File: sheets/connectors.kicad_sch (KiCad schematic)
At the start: 9 parts

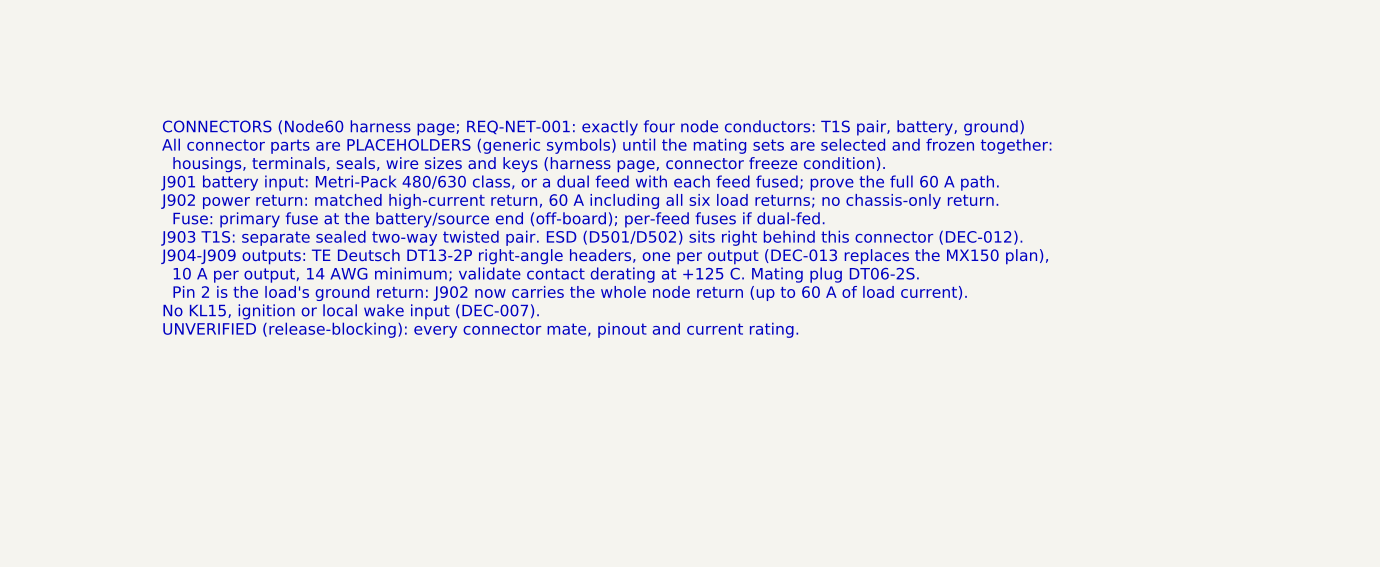
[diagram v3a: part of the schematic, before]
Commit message: Schematic: LHI to the MCU, current notes, net-name map
- LHI on all three TPS2HCS08 is now SW_LHI from S32K344 PTE4 (the
  architecture's GPIO list), still held low by the 10k pull-downs
  through reset.
- Page 4 cites NXP HDG Rev E2 Table 33 for unused GPIO, EXTAL/XTAL and
  the RESET_B pull-up instead of an open 'confirm' note.
- Copper notes for the 10 A output paths (p6) and the 60 A path (p2,
  p9), as IPC-2221 starting estimates to confirm with IPC-2152.
- interfaces.mdx maps the architecture's signal names to the schematic
  nets (RESET_L, T1S_IRQ_L, *_FLT_L, SPI4/SPI2/I2C0 buses).

Co-Authored-By: Claude Opus 5.5 <noreply@anthropic.com>
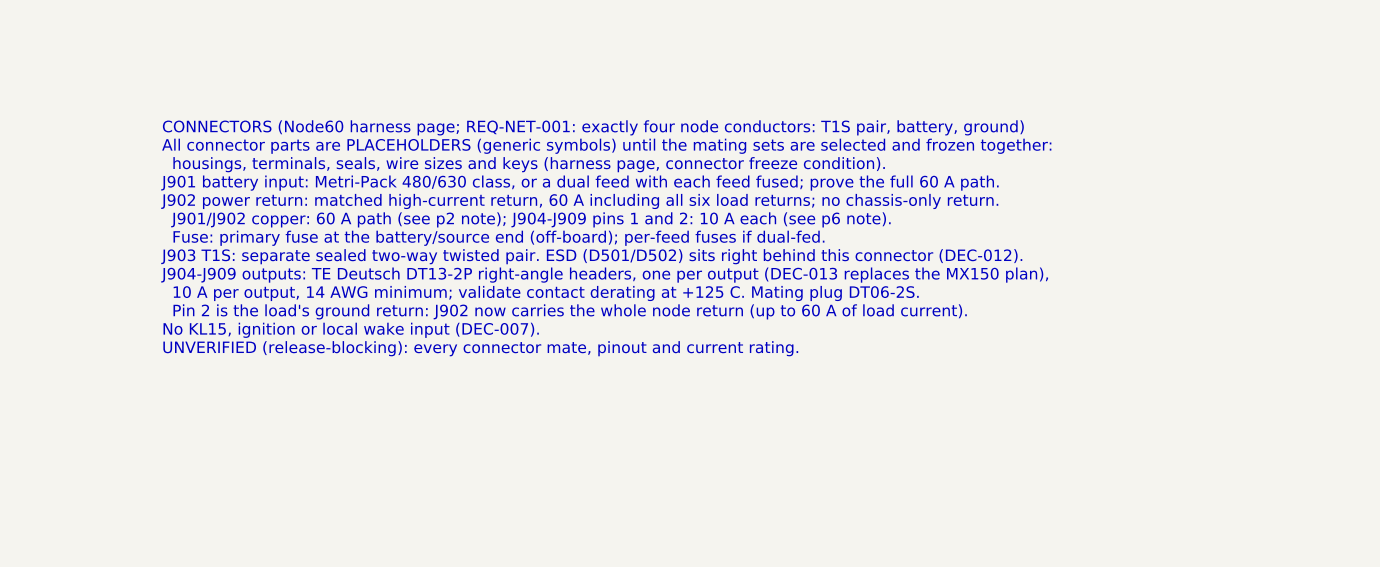
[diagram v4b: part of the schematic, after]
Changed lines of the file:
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@@
 		)
 	)
-	(text "CONNECTORS (Node60 harness page; REQ-NET-001: exactly four node conductors: T1S pair, battery, ground)\nAll connector parts are PLACEHOLDERS (generic symbols) until the mating sets are selected and frozen together:\n  housings, terminals, seals, wire sizes and keys (harness page, connector freeze condition).\nJ901 battery input: Metri-Pack 480/630 class, or a dual feed with each feed fused; prove the full 60 A path.\nJ902 power return: matched high-current return, 60 A including all six load returns; no chassis-only return.\n  Fuse: primary fuse at the battery/source end (off-board); per-feed fuses if dual-fed.\nJ903 T1S: separate sealed two-way twisted pair. ESD (D501/D502) sits right behind this connector (DEC-012).\nJ904-J909 outputs: TE Deutsch DT13-2P right-angle headers, one per output (DEC-013 replaces the MX150 plan),\n  10 A per output, 14 AWG minimum; validate contact derating at +125 C. Mating plug DT06-2S.\n  Pin 2 is the load's ground return: J902 now carries the whole node return (up to 60 A of load current).\nNo KL15, ignition or local wake input (DEC-007).\nUNVERIFIED (release-blocking): every connector mate, pinout and current rating.\n"
+	(text "CONNECTORS (Node60 harness page; REQ-NET-001: exactly four node conductors: T1S pair, battery, ground)\nAll connector parts are PLACEHOLDERS (generic symbols) until the mating sets are selected and frozen together:\n  housings, terminals, seals, wire sizes and keys (harness page, connector freeze condition).\nJ901 battery input: Metri-Pack 480/630 class, or a dual feed with each feed fused; prove the full 60 A path.\nJ902 power return: matched high-current return, 60 A including all six load returns; no chassis-only return.\n  J901/J902 copper: 60 A path (see p2 note); J904-J909 pins 1 and 2: 10 A each (see p6 note).\n  Fuse: primary fuse at the battery/source end (off-board); per-feed fuses if dual-fed.\nJ903 T1S: separate sealed two-way twisted pair. ESD (D501/D502) sits right behind this connector (DEC-012).\nJ904-J909 outputs: TE Deutsch DT13-2P right-angle headers, one per output (DEC-013 replaces the MX150 plan),\n  10 A per output, 14 AWG minimum; validate contact derating at +125 C. Mating plug DT06-2S.\n  Pin 2 is the load's ground return: J902 now carries the whole node return (up to 60 A of load current).\nNo KL15, ignition or local wake input (DEC-007).\nUNVERIFIED (release-blocking): every connector mate, pinout and current rating.\n"
 		(exclude_from_sim no)
 		(at 190.5 116.84 0)

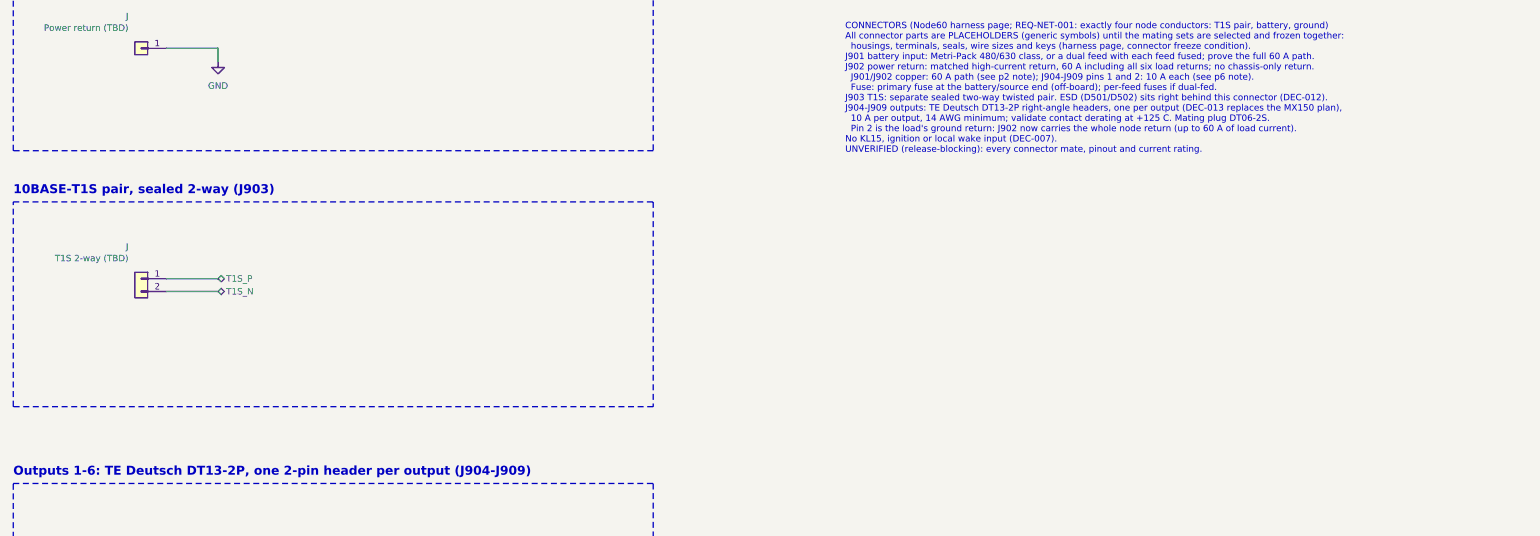
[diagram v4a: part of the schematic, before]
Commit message: Connectors: J903 is the Amphenol SINE ATM13-2P-BM04 (DEC-014)
T1S_P on pin 1, T1S_N on pin 2, with the ESD diodes right behind the
connector per DEC-012. Pin 1 must be verified on a sample
(release-blocking, noted on the sheet).

The library submodule is TEMPORARILY pinned to dropout-kicad-library
PR #26's head (9d70e7f, which contains main 752b63c) for
DropOut_Connector:ATM13-2P-BM04; re-pin to library main once #26
merges. Adds the DropOut_Connector_Amphenol footprint library.

Co-Authored-By: Claude Opus 5.5 <noreply@anthropic.com>
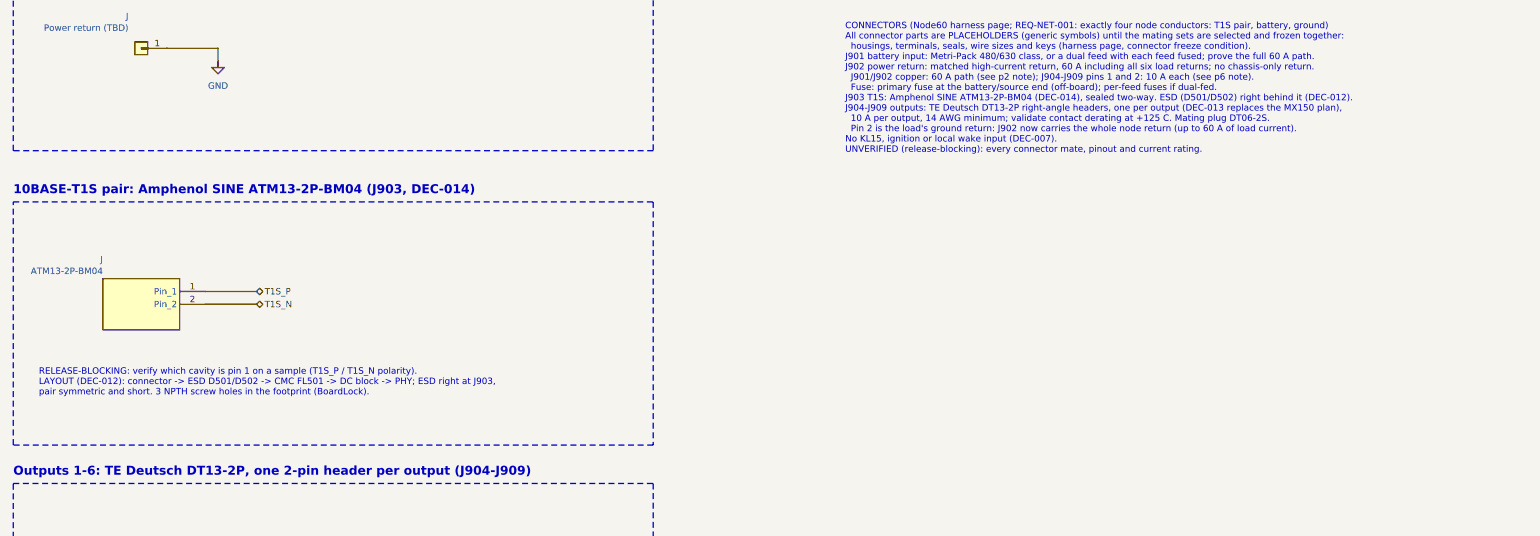
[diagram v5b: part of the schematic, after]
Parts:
- J: value T1S 2-way (TBD) -> ATM13-2P-BM04; footprint (none) -> DropOut_Connector_Amphenol:Amphenol_SINE_ATM13-2P-BMxx_1x02_P4.20mm_Horizontal; symbol Connector_Generic:Conn_01x02 -> DropOut_Connector:ATM13-2P-BM04; DigiKey_PN (none) -> 889-3357-ND; MPN (none) -> ATM13-2P-BM04; Manufacturer (none) -> Amphenol SINE Systems; Mouser_PN (none) -> 654-ATM13-2P-BM04; Notes (none) -> Mates the ATM06-2S plug (size 20 sockets). Fixed by 3x; Placeholder PLACEHOLDER: TBD part: selection pending user decision (fin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 -> (none); Temperature_Grade (none) -> -55 to +125 °C (not AEC qualified)
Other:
- note added: "10BASE-T1S pair: Amphenol SINE ATM13-2P-BM04 (J903, DEC-014)"
- note added: "RELEASE-BLOCKING: verify which cavity is pin 1 on a sample (T1S_P / T1S_N polarity). LAYOUT (DEC-012): connector -> ESD D501/D502 -> CMC FL501 -> DC block -> PHY; ESD right at J903, pair symmetric and short. 3 NPTH screw holes in the footprint (BoardLock)."
- note removed: "10BASE-T1S pair, sealed 2-way (J903)"
- moved on the sheet: J
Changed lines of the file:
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@@
 	(rectangle
 		(start 25.4 152.4)
-		(end 152.4 193.04)
+		(end 152.4 200.66)
 		(stroke
 			(width 0.254)
@@
 		)
 	)
-	(text "10BASE-T1S pair, sealed 2-way (J903)"
+	(text "10BASE-T1S pair: Amphenol SINE ATM13-2P-BM04 (J903, DEC-014)"
 		(exclude_from_sim no)
 		(at 25.4 151.13 0)
@@
 	)
 	(symbol
-		(lib_id "Connector_Generic:Conn_01x02")
-		(at 50.8 167.64 0)
+		(lib_id "DropOut_Connector:ATM13-2P-BM04")
+		(at 50.8 172.72 0)
 		(mirror y)
 		(unit 1)
@@
 		(fields_autoplaced no)
 		(property "Reference" "J"
-			(at 48.26 161.29 0)
+			(at 43.18 163.83 0)
 			(effects
 				(font
@@
 			)
 		)
-		(property "Value" "T1S 2-way (TBD)"
-			(at 48.26 163.59 0)
+		(property "Value" "ATM13-2P-BM04"
+			(at 43.18 166.13 0)
 			(effects
 				(font
@@
 			)
 		)
-		(property "Footprint" ""
-			(at 50.8 167.64 0)
-			(effects
-				(font
-					(size 1.27 1.27)
-				)
-				(hide yes)
-			)
-		)
-		(property "Datasheet" ""
-			(at 50.8 167.64 0)
-			(effects
-				(font
-					(size 1.27 1.27)
-				)
-				(hide yes)
-			)
-		)
-		(property "Description" "Generic connector, single row, 01x02, script generated (kicad-library-utils/schlib/autogen/connector/)"
-			(at 50.8 167.64 0)
-			(effects
-				(font
-					(size 1.27 1.27)
-				)
-				(hide yes)
-			)
-		)
-		(property "MPN" ""
-			(at 50.8 167.64 0)
-			(effects
-				(font
-					(size 1.27 1.27)
-				)
-				(hide yes)
-			)
-		)
-		(property "Manufacturer" ""
-			(at 50.8 167.64 0)
-			(effects
-				(font
-					(size 1.27 1.27)
-				)
-				(hide yes)
-			)
-		)
-		(property "DigiKey_PN" ""
-			(at 50.8 167.64 0)
-			(effects
-				(font
-					(size 1.27 1.27)
-				)
-				(hide yes)
-			)
-		)
-		(property "Mouser_PN" ""
-			(at 50.8 167.64 0)
-			(effects
-				(font
-					(size 1.27 1.27)
-				)
-				(hide yes)
-			)
-		)
-		(property "Placeholder" "PLACEHOLDER: TBD part: selection pending user decision (find-part), then a library session (separate sealed two-way twisted pair)"
-			(at 50.8 167.64 0)
+		(property "Footprint" "DropOut_Connector_Amphenol:Amphenol_SINE_ATM13-2P-BMxx_1x02_P4.20mm_Horizontal"
+			(at 50.8 172.72 0)
+			(effects
+				(font
+					(size 1.27 1.27)
+				)
+				(hide yes)
+			)
+		)
+		(property "Datasheet" "https://www.amphenol-sine.com/pdf/datasheet/ATM13-2P-BM04.pdf"
+			(at 50.8 172.72 0)
+			(effects
+				(font
+					(size 1.27 1.27)
+				)
+				(hide yes)
+			)
+		)
+		(property "Description" "Amphenol SINE BoardLock ATM13 2-pin right-angle PCB receptacle with flange seal, 4.20 mm pitch, tin-plated size 20 pins, potting, 7.5 A, 250 V, IP67 mated, -55 to +125 °C; mates ATM06-2S"
+			(at 50.8 172.72 0)
+			(effects
+				(font
+					(size 1.27 1.27)
+				)
+				(hide yes)
+			)
+		)
+		(property "Manufacturer" "Amphenol SINE Systems"
+			(at 50.8 172.72 0)
+			(effects
+				(font
+					(size 1.27 1.27)
+				)
+				(hide yes)
+			)
+		)
+		(property "MPN" "ATM13-2P-BM04"
+			(at 50.8 172.72 0)
+			(effects
+				(font
+					(size 1.27 1.27)
+				)
+				(hide yes)
+			)
+		)
+		(property "DigiKey_PN" "889-3357-ND"
+			(at 50.8 172.72 0)
+			(effects
+				(font
+					(size 1.27 1.27)
+				)
+				(hide yes)
+			)
+		)
+		(property "Mouser_PN" "654-ATM13-2P-BM04"
+			(at 50.8 172.72 0)
+			(effects
+				(font
+					(size 1.27 1.27)
+				)
+				(hide yes)
+			)
+		)
+		(property "Temperature_Grade" "-55 to +125 °C (not AEC qualified)"
+			(at 50.8 172.72 0)
+			(effects
+				(font
+					(size 1.27 1.27)
+				)
+				(hide yes)
+			)
+		)
+		(property "Notes" "Mates the ATM06-2S plug (size 20 sockets). Fixed by 3x"
+			(at 50.8 172.72 0)
 			(effects
 				(font
@@
 	(wire
 		(pts
-			(xy 55.88 167.64)
-			(xy 66.04 167.64)
+			(xy 63.5 170.18)
+			(xy 73.66 170.18)
 		)
 		(stroke
@@
 	(hierarchical_label "T1S_P"
 		(shape bidirectional)
-		(at 66.04 167.64 0)
+		(at 73.66 170.18 0)
 		(effects
 			(font
@@
 	(wire
 		(pts
-			(xy 55.88 170.18)
-			(xy 66.04 170.18)
+			(xy 63.5 172.72)
+			(xy 73.66 172.72)
 		)
 		(stroke
@@
 	(hierarchical_label "T1S_N"
 		(shape bidirectional)
-		(at 66.04 170.18 0)
+		(at 73.66 172.72 0)
 		(effects
 			(font
@@
 			)
 			(justify left)
+		)
+	)
+	(text "RELEASE-BLOCKING: verify which cavity is pin 1 on a sample (T1S_P / T1S_N polarity).\nLAYOUT (DEC-012): connector -> ESD D501/D502 -> CMC FL501 -> DC block -> PHY; ESD right at J903,\npair symmetric and short. 3 NPTH screw holes in the footprint (BoardLock)."
+		(exclude_from_sim no)
+		(at 30.48 185.42 0)
+		(effects
+			(font
+				(size 1.27 1.27)
+			)
+			(justify left top)
 		)
 	)
@@
 		)
 	)
-	(text "CONNECTORS (Node60 harness page; REQ-NET-001: exactly four node conductors: T1S pair, battery, ground)\nAll connector parts are PLACEHOLDERS (generic symbols) until the mating sets are selected and frozen together:\n  housings, terminals, seals, wire sizes and keys (harness page, connector freeze condition).\nJ901 battery input: Metri-Pack 480/630 class, or a dual feed with each feed fused; prove the full 60 A path.\nJ902 power return: matched high-current return, 60 A including all six load returns; no chassis-only return.\n  J901/J902 copper: 60 A path (see p2 note); J904-J909 pins 1 and 2: 10 A each (see p6 note).\n  Fuse: primary fuse at the battery/source end (off-board); per-feed fuses if dual-fed.\nJ903 T1S: separate sealed two-way twisted pair. ESD (D501/D502) sits right behind this connector (DEC-012).\nJ904-J909 outputs: TE Deutsch DT13-2P right-angle headers, one per output (DEC-013 replaces the MX150 plan),\n  10 A per output, 14 AWG minimum; validate contact derating at +125 C. Mating plug DT06-2S.\n  Pin 2 is the load's ground return: J902 now carries the whole node return (up to 60 A of load current).\nNo KL15, ignition or local wake input (DEC-007).\nUNVERIFIED (release-blocking): every connector mate, pinout and current rating.\n"
+	(text "CONNECTORS (Node60 harness page; REQ-NET-001: exactly four node conductors: T1S pair, battery, ground)\nAll connector parts are PLACEHOLDERS (generic symbols) until the mating sets are selected and frozen together:\n  housings, terminals, seals, wire sizes and keys (harness page, connector freeze condition).\nJ901 battery input: Metri-Pack 480/630 class, or a dual feed with each feed fused; prove the full 60 A path.\nJ902 power return: matched high-current return, 60 A including all six load returns; no chassis-only return.\n  J901/J902 copper: 60 A path (see p2 note); J904-J909 pins 1 and 2: 10 A each (see p6 note).\n  Fuse: primary fuse at the battery/source end (off-board); per-feed fuses if dual-fed.\nJ903 T1S: Amphenol SINE ATM13-2P-BM04 (DEC-014), sealed two-way. ESD (D501/D502) right behind it (DEC-012).\nJ904-J909 outputs: TE Deutsch DT13-2P right-angle headers, one per output (DEC-013 replaces the MX150 plan),\n  10 A per output, 14 AWG minimum; validate contact derating at +125 C. Mating plug DT06-2S.\n  Pin 2 is the load's ground return: J902 now carries the whole node return (up to 60 A of load current).\nNo KL15, ignition or local wake input (DEC-007).\nUNVERIFIED (release-blocking): every connector mate, pinout and current rating.\n"
 		(exclude_from_sim no)
 		(at 190.5 116.84 0)

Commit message: Re-pin library to PR #26 head cfea26e (renamed ATM13 footprint)
J903's footprint is now
DropOut_Connector_Amphenol:Amphenol_ATM13-2P-BMxx_1x02_P4.20mm_Horizontal.
Still a temporary pin: move to library main once #26 merges.

Co-Authored-By: Claude Opus 5.5 <noreply@anthropic.com>
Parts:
- J: footprint DropOut_Connector_Amphenol:Amphenol_SINE_ATM13-2P-BMxx_1x02_P4.20mm_Horizontal -> DropOut_Connector_Amphenol:Amphenol_ATM13-2P-BMxx_1x02_P4.20mm_Horizontal
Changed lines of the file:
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@@
 			)
 		)
-		(property "Footprint" "DropOut_Connector_Amphenol:Amphenol_SINE_ATM13-2P-BMxx_1x02_P4.20mm_Horizontal"
+		(property "Footprint" "DropOut_Connector_Amphenol:Amphenol_ATM13-2P-BMxx_1x02_P4.20mm_Horizontal"
 			(at 50.8 172.72 0)
 			(effects

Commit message: Outputs J904-J909: Amphenol Sine AT13-2P-BM04 (DEC-013 rev. B)
Replaces the TE DT13-2P per DEC-013 rev. B (node60-hw PR #10). Pin
assignment unchanged: pin 1 = OUTx, pin 2 = that load's ground return.
Library pinned to PR #26's head 18a8718, which merges library main and
so contains both #25 (AT13-2P-BM04) and #26 (ATM13-2P-BM04, J903).
Still temporary: move to library main once #26 merges.

Co-Authored-By: Claude Opus 5.5 <noreply@anthropic.com>
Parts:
- J: value DT13-2P -> AT13-2P-BM04; footprint DropOut_Connector_TE-Connectivity:TE_DEUTSCH-DT_DT13-2P_1x02_P5.46mm_Horizontal -> DropOut_Connector_Amphenol:Amphenol_AT13-2P-BMxx_1x02_P5.40mm_Horizontal; symbol DropOut_Connector:DT13-2P -> DropOut_Connector:AT13-2P-BM04; DigiKey_PN 1734-1452-ND -> 889-3345-ND; MPN DT13-2P -> AT13-2P-BM04; Manufacturer TE Connectivity -> Amphenol Sine Systems; Mouser_PN 571-DT13-2P -> 654-AT13-2P-BM04; Notes Mates DT06-2S + W2S wedgelock. No current derating curve; +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 -> Mates AT06-2S plug (DT06-2S compatible). Potted version, ra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; Temperature_Grade -55 to +125 °C (not AEC qualified) -> -55 to +125 °C at rated current (not AEC qualified)
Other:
- note added: "Outputs 1-6: Amphenol Sine AT13-2P-BM04, one 2-pin header per output (J904-J909)"
- note added: "Pin 1 = OUTx, pin 2 = that load's ground return (DEC-013 rev. B: AT13-2P-BM04, 5.40 mm pitch). LAYOUT: each pin 2 return carries up to 10 A, like its OUTx: same copper and via treatment. Route pin 2 returns to the power-entry ground star region, never across the logic ground. Up to 60 A of load return flows from the headers to the star region and out through J902. RELEASE-BLOCKING: verify which c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"
- note removed: "Outputs 1-6: TE Deutsch DT13-2P, one 2-pin header per output (J904-J909)"
- note removed: "Pin 1 = OUTx, pin 2 = that load's ground return (DEC-013, decided 2026-10-22). LAYOUT: each pin 2 return carries up to 10 A, like its OUTx: same copper and via treatment. Route pin 2 returns to the power-entry ground star region, never across the logic ground. Up to 60 A of load return flows from the headers to the star region and out through J902. RELEASE-BLOCKING: which physical hole is pin 1 (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"
